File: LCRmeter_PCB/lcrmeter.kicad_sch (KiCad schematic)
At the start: 55 parts, among them J1 UART, J2 Prog_interface, J3 misc, J4 misc, J5 LCR_input, J6 LCR_input, SW1 power, SW2 ok, SW3 back, SW4 up, SW5 down, U1 Mylibrary_OLED, U2 74HC14, U3 STM32G473C_B-C-E_Tx

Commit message: PCB and schematic update for next version
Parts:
- added C48: 10u, Capacitor_SMD:C_0805_2012Metric_Pad1.18x1.45mm_HandSolder, symbol Device:C
- added H1: M, MountingHole:MountingHole_3.2mm_M3_ISO14580, symbol Mechanical:MountingHole
- C1: value 10u -> 20u
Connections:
- net +BATT is gone; now on net VCC: SW1.3
- net BUTTON_BACK: now also U3.17 (PB1); no longer U3.42 (PB5)
- net BUTTON_OK: now also U3.18 (PB2); no longer U3.41 (PB4)
- net EN_PATH_1: now also U3.34 (PA12); no longer U3.28 (PB14)
- net EN_PATH_2: now also U3.30 (PA8); no longer U3.43 (PB6)
- net EN_PATH_3: now also U3.29 (PB15); no longer U3.46 (PB9)
- net EN_PATH_4: now also U3.28 (PB14); no longer U3.29 (PB15)
- net GND: now also C48.2
- net PWM_OUT: now also U3.33 (PA11); no longer U3.34 (PA12)
- net USART_RX: now also J1.2 (Pin_2); no longer J1.3 (Pin_3)
- net USART_TX: now also J1.3 (Pin_3), U3.31 (PA9); no longer J1.2 (Pin_2), U3.33 (PA11)
- net VCC: now also C1.1, C48.1
- net Vg_FILTERED: now also U3.11 (PA3); no longer U3.10 (PA2)
- net at BT1.1 (+), SW1.2: no longer C1.1
- net BUTTON_UP: now reaches U3.15 (PA7)
- net BUTTON_UP: now also U2.2
- net BUTTON_DOWN: now reaches U3.16 (PB0)
- net BUTTON_DOWN: now also U2.4
- removed net BUTTON_+: U2.2, U3.18 (PB2)
- removed net BUTTON_-: U2.4, U3.17 (PB1)
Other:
- note added: "placeholder"

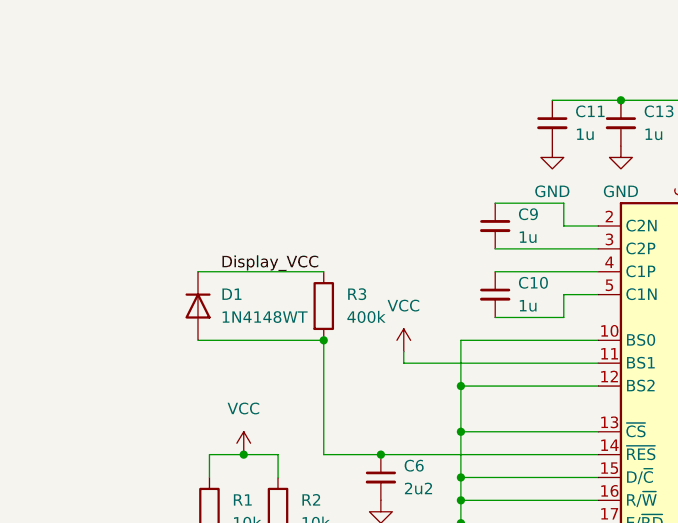
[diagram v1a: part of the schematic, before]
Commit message: fix pcb and oled connection
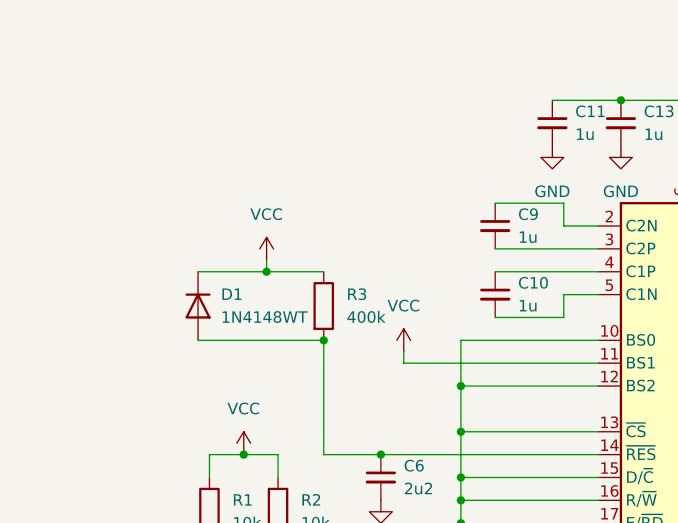
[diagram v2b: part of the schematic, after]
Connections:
- net Display_VCC: no longer D1.1 (K), R3.1
- net VCC: now also D1.1 (K), R3.1
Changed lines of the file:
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@@
 	)
 	(junction
+		(at 38.1 40.64)
+		(diameter 0)
+		(color 0 0 0 0)
+	)
+	(junction
 		(at 39.37 73.66)
 		(diameter 0)
@@
 	(wire
 		(pts
+			(xy 38.1 40.64) (xy 38.1 39.37)
+		)
+		(stroke
+			(width 0)
+			(type default)
+		)
+	)
+	(wire
+		(pts
 			(xy 208.28 107.95) (xy 208.28 110.49)
 		)
@@
 	(wire
 		(pts
+			(xy 30.48 40.64) (xy 38.1 40.64)
+		)
+		(stroke
+			(width 0)
+			(type default)
+		)
+	)
+	(wire
+		(pts
 			(xy 71.12 35.56) (xy 71.12 33.02)
 		)
@@
 	(wire
 		(pts
+			(xy 44.45 40.64) (xy 38.1 40.64)
+		)
+		(stroke
+			(width 0)
+			(type default)
+		)
+	)
+	(wire
+		(pts
 			(xy 196.85 160.02) (xy 196.85 158.75)
 		)
@@
 	(wire
 		(pts
-			(xy 30.48 40.64) (xy 44.45 40.64)
-		)
-		(stroke
-			(width 0)
-			(type default)
-		)
-	)
-	(wire
-		(pts
 			(xy 275.59 69.85) (xy 274.32 69.85)
 		)
@@
 		)
 	)
-	(label "Display_VCC"
-		(at 33.02 40.64 0)
-		(effects
-			(font
-				(size 1.27 1.27)
-			)
-			(justify left bottom)
-		)
-	)
 	(label "EN_PATH_4"
 		(at 187.96 97.79 180)
@@
 			)
 		)
-		(property "Datasheet" ""
+		(property "Datasheet" "~"
 			(at 101.6 148.336 90)
 			(effects
@@
 			)
 		)
+		(property "Sim.Device" "V"
+			(at 101.6 149.86 0)
+			(effects
+				(font
+					(size 1.27 1.27)
+				)
+				(hide yes)
+			)
+		)
+		(property "Sim.Type" "DC"
+			(at 101.6 149.86 0)
+			(effects
+				(font
+					(size 1.27 1.27)
+				)
+				(hide yes)
+			)
+		)
+		(property "Sim.Pins" "1=+ 2=-"
+			(at 101.6 149.86 0)
+			(effects
+				(font
+					(size 1.27 1.27)
+				)
+				(hide yes)
+			)
+		)
 		(pin "1"
 		)
@@
 					(unit 1)
 				)
+			)
+		)
+	)
+	(symbol
+		(lib_id "power:VCC")
+		(at 38.1 39.37 0)
+		(unit 1)
+		(exclude_from_sim no)
+		(in_bom yes)
+		(on_board yes)
+		(dnp no)
+		(fields_autoplaced yes)
+		(property "Reference" "#PWR015"
+			(at 38.1 43.18 0)
+			(effects
+				(font
+					(size 1.27 1.27)
+				)
+				(hide yes)
+			)
+		)
+		(property "Value" "VCC"
+			(at 38.1 34.29 0)
+			(effects
+				(font
+					(size 1.27 1.27)
+				)
+			)
+		)
+		(property "Footprint" ""
+			(at 38.1 39.37 0)
+			(effects
+				(font
+					(size 1.27 1.27)
+				)
+				(hide yes)
+			)
+		)
+		(property "Datasheet" ""
+			(at 38.1 39.37 0)
+			(effects
+				(font
+					(size 1.27 1.27)
+				)
+				(hide yes)
+			)
+		)
+		(property "Description" "Power symbol creates a global label with name \"VCC\""
+			(at 38.1 39.37 0)
+			(effects
+				(font
+					(size 1.27 1.27)
+				)
+				(hide yes)
+			)
+		)
+		(pin "1"
+		)
+		(instances
+			(project "lcrmeter"
+				(path "/cf9a12ad-2fa3-4d0e-8bc4-f65b698e427e"
+					(reference "#PWR015")
+					(unit 1)
+				)
